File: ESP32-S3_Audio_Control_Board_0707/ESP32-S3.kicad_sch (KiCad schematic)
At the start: 25 parts, among them U1 ESP32-S3-WROOM-1

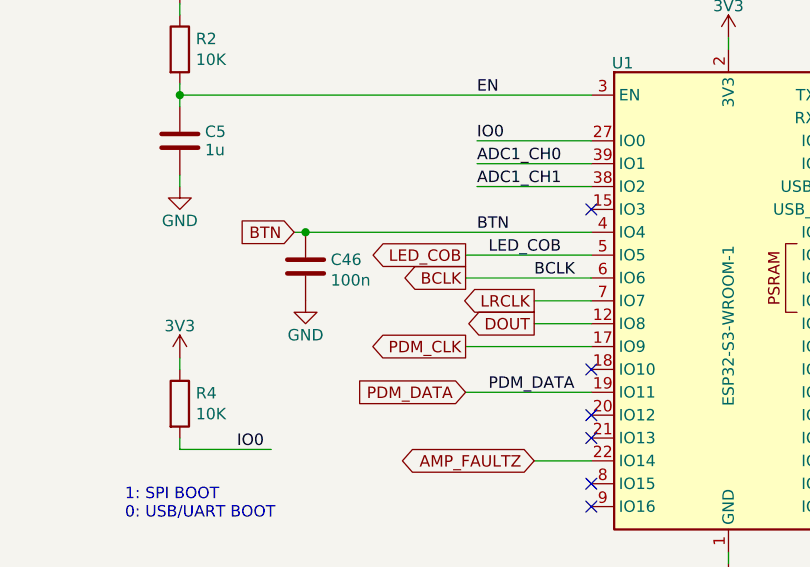
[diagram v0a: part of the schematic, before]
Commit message: update TAS5805, 4-layer
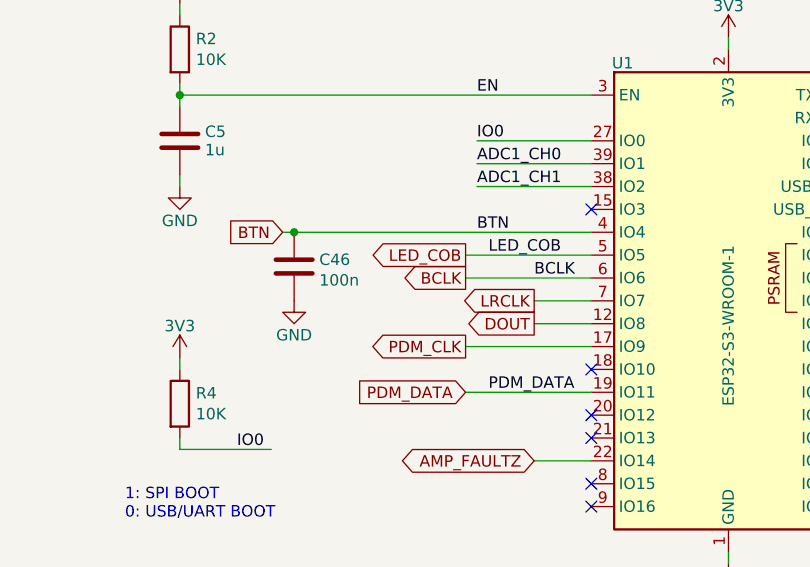
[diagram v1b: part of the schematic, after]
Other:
- moved on the sheet: C46
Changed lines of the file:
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@@
 	)
 	(junction
-		(at 105.41 100.33)
+		(at 104.14 100.33)
 		(diameter 0)
 		(color 0 0 0 0)
@@
 	(wire
 		(pts
-			(xy 105.41 100.33) (xy 137.16 100.33)
+			(xy 104.14 100.33) (xy 137.16 100.33)
 		)
 		(stroke
@@
 	(wire
 		(pts
-			(xy 104.14 100.33) (xy 105.41 100.33)
+			(xy 102.87 100.33) (xy 104.14 100.33)
 		)
 		(stroke
@@
 	(global_label "BTN"
 		(shape input)
-		(at 104.14 100.33 180)
+		(at 102.87 100.33 180)
 		(fields_autoplaced yes)
 		(effects
@@
 		)
 		(property "Intersheetrefs" "${INTERSHEET_REFS}"
-			(at 97.5867 100.33 0)
+			(at 96.3167 100.33 0)
 			(hide yes)
 			(show_name no)
@@
 	(symbol
 		(lib_id "SparkFun-PowerSymbol:GND")
-		(at 105.41 107.95 0)
+		(at 104.14 107.95 0)
 		(unit 1)
 		(body_style 1)
@@
 		(dnp no)
 		(property "Reference" "#PWR040"
-			(at 105.41 114.3 0)
+			(at 104.14 114.3 0)
 			(hide yes)
 			(show_name no)
@@
 		)
 		(property "Value" "GND"
-			(at 105.41 111.76 0)
+			(at 104.14 111.76 0)
 			(show_name no)
 			(do_not_autoplace no)
@@
 		)
 		(property "Footprint" ""
-			(at 105.41 107.95 0)
+			(at 104.14 107.95 0)
 			(hide yes)
 			(show_name no)
@@
 		)
 		(property "Datasheet" ""
-			(at 105.41 107.95 0)
+			(at 104.14 107.95 0)
 			(hide yes)
 			(show_name no)
@@
 		)
 		(property "Description" ""
-			(at 105.41 107.95 0)
+			(at 104.14 107.95 0)
 			(show_name no)
 			(do_not_autoplace no)
@@
 	(symbol
 		(lib_id "Device:C")
-		(at 105.41 104.14 0)
+		(at 104.14 104.14 0)
 		(unit 1)
 		(body_style 1)
@@
 		(dnp no)
 		(property "Reference" "C46"
-			(at 108.204 103.378 0)
+			(at 106.934 103.378 0)
 			(show_name no)
 			(do_not_autoplace no)
@@
 		)
 		(property "Value" "100n"
-			(at 108.204 105.664 0)
+			(at 106.934 105.664 0)
 			(show_name no)
 			(do_not_autoplace no)
@@
 		)
 		(property "Footprint" "Capacitor_SMD:C_0402_1005Metric"
-			(at 106.3752 107.95 0)
+			(at 105.1052 107.95 0)
 			(hide yes)
 			(show_name no)
@@
 		)
 		(property "Datasheet" "https://jlc-prod-smt.oss-eu-central-1.aliyuncs.com/smtDataManualFile/8588933581779709952-C71687.pdf?response-content-disposition=attachment%3B%20filename%3DC71687.pdf%3B%20filename%2A%3DUTF-8%27%27C71687.pdf&x-oss-date=20260701T135229Z&x-oss-expires=3600&x-oss-security-token=CAISgAN1q6Ft5B2yfSjIr5nxCsvRl4cT1rujb2GJgXJgf9t2gofClzz2IHhMdHJsAOodtv0%2FmmhT6PkclqRLcbhpcmfjV%2BZHzLB8qdtdtBBY4J7b16cNrbH4M4H6aXeirtuwDsz9SNTCALjPD3nPii50x5bjaDymRCbLGJaViJlhHLN1Ow6jdmhpCctxLAlvo9NgFxm3D%2Fu2NQPwiWf9FVdhvhEG6Vly8qOi2MaRmFy8yFTx0b0SvJ%2BjYMrmPctoN9JnSdC5mfdzau3a1TJ84gRD0a5wkaVA1zbDs5bfISEIuUzebreLqY03dV4mOvdqIcMe8qigz88fk%2FfIioH6xyxKOexoSCnFTOiiupCcQLPyao9jLu6iayqViY7QaIOTqQohZmkAMwVOasAsI3Ngh4zF97Qt0cVNkXO9gWfLI8DtuMleWiptDMB90tHD0eS19jklBdzSlusJRAJJUVBflCeKEaRNSAd3WGhEfM2%2BBt4QT30w5N2u00S8OSMIEKL%2FAKKWD5sagAEPEI%2BnXsiosgKaOvk01oQiVJPGVRrKu%2FrEk42ZNlnsDQBAF0efd5V9lCOR%2FqDuWGuZZY6Hm%2BUNg9NLzWBzt%2B3Y5omRQ8OaZTBChIakZE1pZEgG%2BOl5oG8Ru7YUzmx9AfCOiA5eIg%2Fdezg%2Bp5UcC%2BsWFkt%2BvND3e0vQSpTG82D3sSAA&x-oss-signature-version=OSS4-HMAC-SHA256&x-oss-credential=STS.NZDAqezX2ayHmG8er5sTZmBiu%2F20260701%2Feu-central-1%2Foss%2Faliyun_v4_request&x-oss-signature=7778ceb79d4aea254572d5565c8cf6986f0b7a0a88a94ed0acb6f0cbd4d4fb81"
-			(at 105.41 104.14 0)
+			(at 104.14 104.14 0)
 			(hide yes)
 			(show_name no)
@@
 		)
 		(property "Description" ""
-			(at 105.41 104.14 0)
+			(at 104.14 104.14 0)
 			(hide yes)
 			(show_name no)
@@
 		)
 		(property "Mfr" "Murata Electronics"
-			(at 105.41 104.14 0)
+			(at 104.14 104.14 0)
 			(hide yes)
 			(show_name no)
@@
 		)
 		(property "Mfr PN" "GCM155R71H104KE02D"
-			(at 105.41 104.14 0)
+			(at 104.14 104.14 0)
 			(hide yes)
 			(show_name no)
@@
 		)
 		(property "Supplier" "LCSC"
-			(at 105.41 104.14 0)
+			(at 104.14 104.14 0)
 			(hide yes)
 			(show_name no)
@@
 		)
 		(property "Supplier PN" "C85858"
-			(at 105.41 104.14 0)
+			(at 104.14 104.14 0)
 			(hide yes)
 			(show_name no)
@@
 		)
 		(property "Part Description" "CAP CER 100nF 50V X7R 0402"
-			(at 105.41 104.14 0)
+			(at 104.14 104.14 0)
 			(hide yes)
 			(show_name no)
@@
 		)
 		(property "PROD_ID" ""
-			(at 105.41 104.14 0)
+			(at 104.14 104.14 0)
 			(hide yes)
 			(show_name no)
